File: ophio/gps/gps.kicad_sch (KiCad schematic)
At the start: 28 parts, among them J1 Conn_01x07, J2 SMA, U1 AP2112K-3.3, U2 TXS0108EPW, U3 LC29H

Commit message: Globally remove LCSC labels, update MPNs and IOCs, add +5V monitoring to DAQs, fix some footprints
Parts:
- U1: LCSC C51118 -> (none)
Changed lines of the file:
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@@
-			)
-		)
-		(property "LCSC" "C51118"
-			(at 74.93 175.26 0)
-			(hide yes)
-			(show_name no)
-			(do_not_autoplace no)
-			(effects
-				(font
-					(size 1.27 1.27)
-				)
 			)
 		)

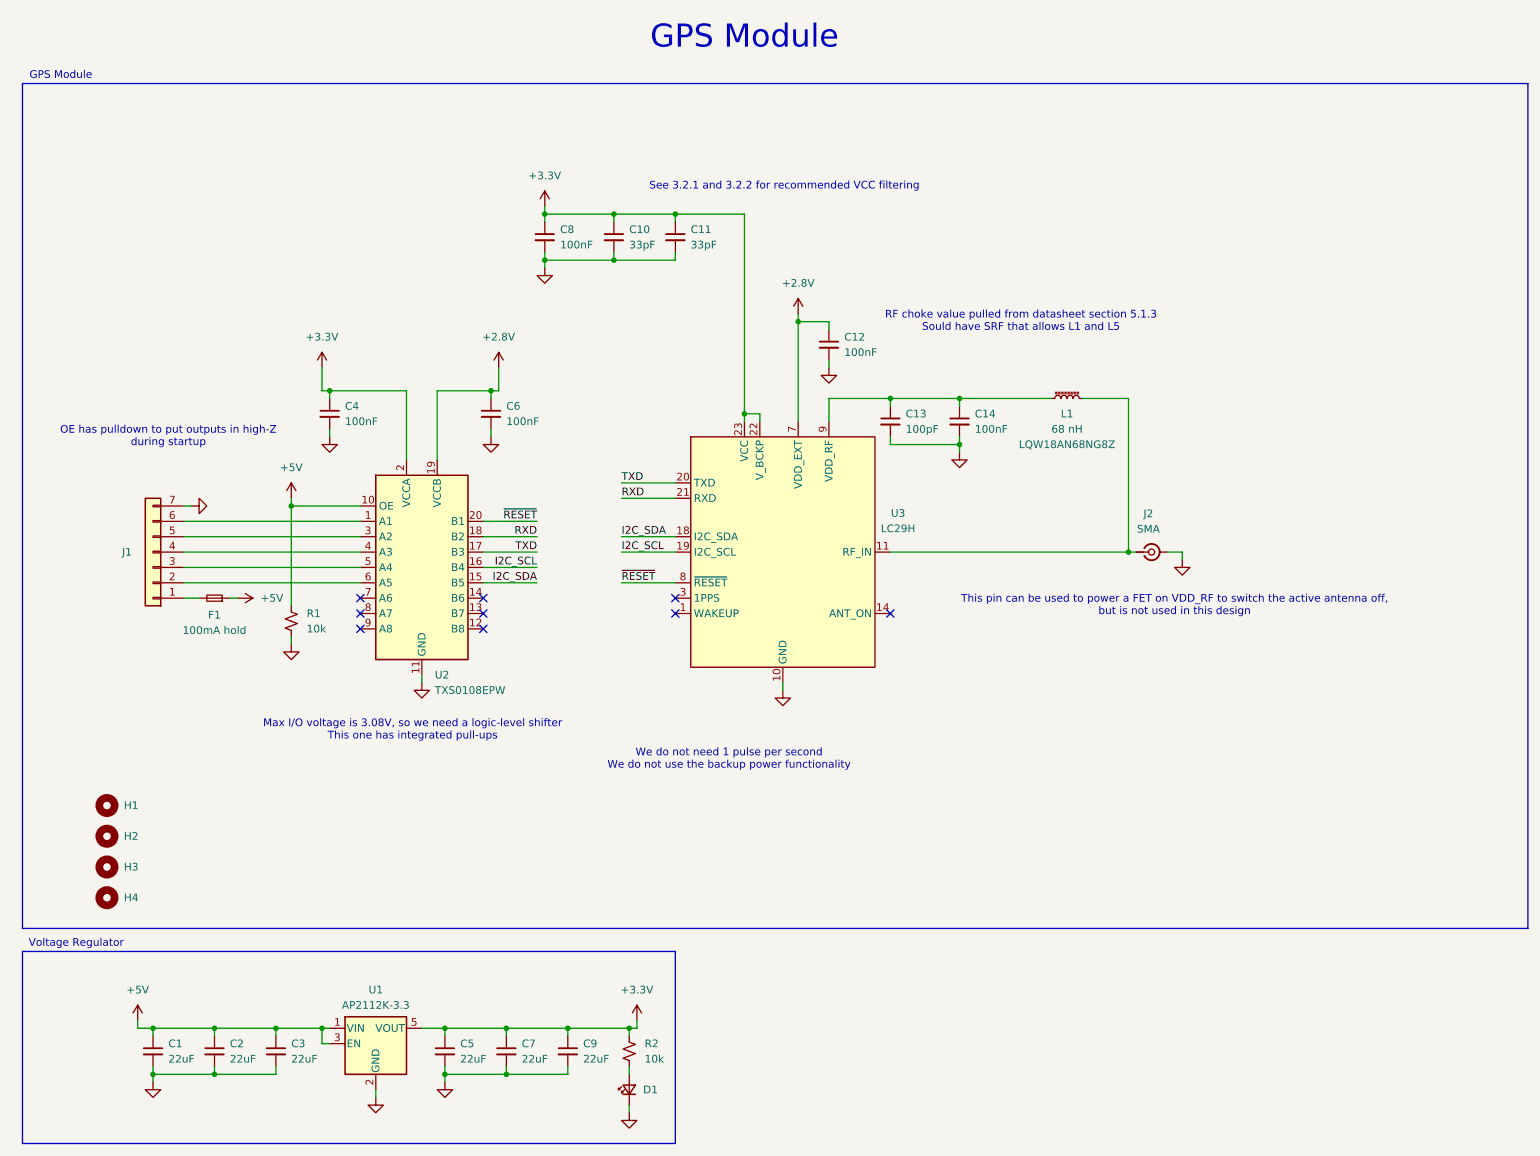
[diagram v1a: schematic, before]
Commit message: the great flatpak and kicad 10.0.6 migration
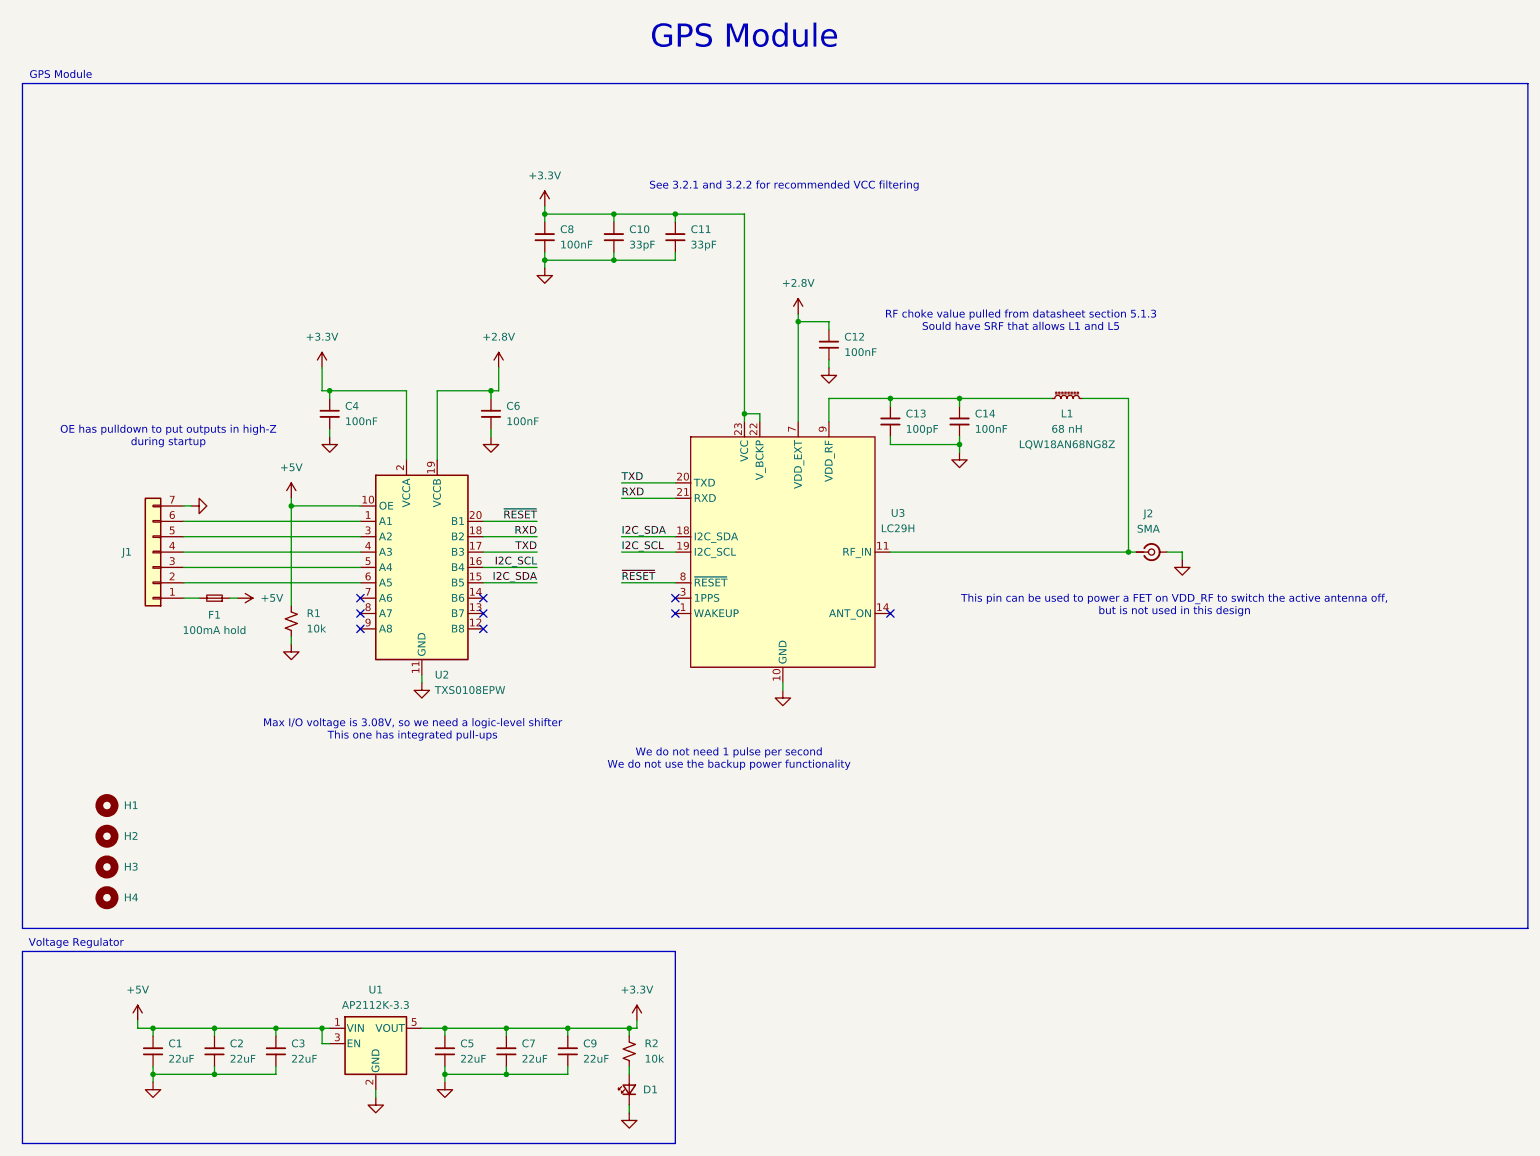
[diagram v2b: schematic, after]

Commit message: Document setup, update template, and use an ampersand when referring to APRL
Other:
- company: Aggie Propulsion and Rocketry Lab -> Aggie Propulsion & Rocketry Lab
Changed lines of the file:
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@@
 		(date "2026-01-18")
 		(rev "1A")
-		(company "Aggie Propulsion and Rocketry Lab")
+		(company "Aggie Propulsion & Rocketry Lab")
 		(comment 1 "Drawn by: Nolan Poe")
 		(comment 2 "Checked by: Daniel Fan")
